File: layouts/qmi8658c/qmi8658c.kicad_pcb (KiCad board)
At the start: 2 copper layers, 3 parts

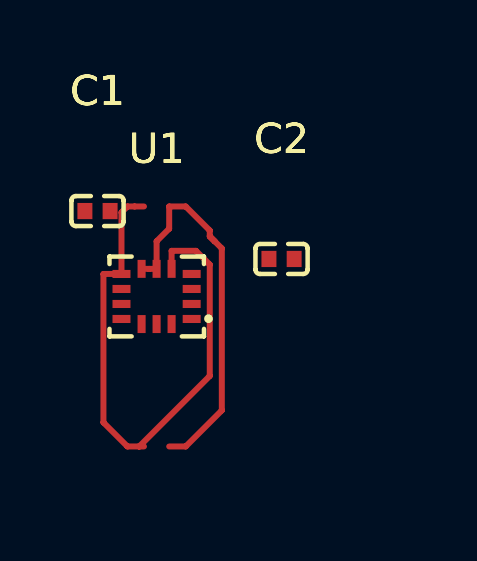
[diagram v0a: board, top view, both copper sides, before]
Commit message: Enhance smart placer with simulated annealing and pre-routing validation
Smart Placer improvements:
- Add simulated annealing refinement (now default) for better wire length optimization
- Add force-directed refinement with improvement safeguard
- Add silkscreen text repositioning to avoid component overlaps
- Significant wire length reductions (e.g., power_filter: 113mm -> 46mm)

Autorouter improvements:
- Add PreRoutingValidator class for pre-flight checks
- Validate unconnected pads, overlapping footprints, unplaced components
- Use pad-based bounds for accurate overlap detection
- Block routing on validation errors with actionable messages

Research:
- Add comprehensive autorouting/autoplacement findings document
- Cover Freerouting Python client, OrthoRoute, DeepPCB, KiCad 9 IPC API
- Document force-directed and simulated annealing algorithms

Cleanup:
- Update .gitignore for DSN/SES files, build artifacts, tools
- Remove stale timestamped build files
- Add parts footprints and symbols

All 10 modules placed and routed successfully.

Co-Authored-By: Claude Opus 4.5 <noreply@anthropic.com>
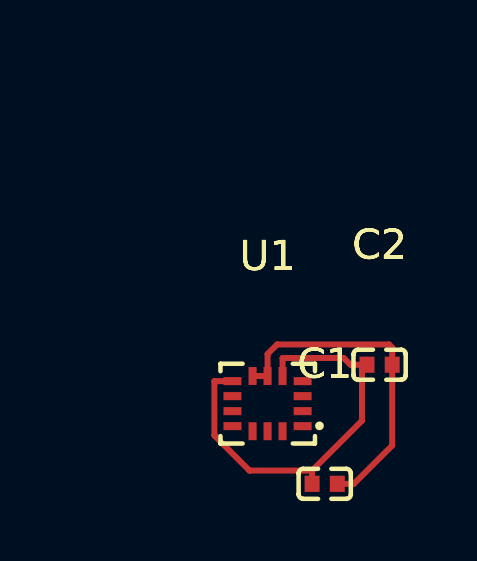
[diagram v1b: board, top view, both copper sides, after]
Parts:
- moved C1 11.8 mm to (105.6, 106.2)
- moved U1 5.14 mm to (103.7, 103.6)
- moved C2 4.81 mm to (107.4, 102.3)
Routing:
- net vcc: track 19.2 -> 14.3 mm
- net gnd: track 13.1 -> 11.2 mm
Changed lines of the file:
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@@
 	(footprint "Samsung_Electro_Mechanics_CL05B104KO5NNNC:C0402"
 		(layer "F.Cu")
-		(at 98.030384 97.152703)
+		(at 105.6041 106.2451)
 		(property "Reference" "C1"
 			(at 0 -4 0)
@@
 	(footprint "QST_QMI8658C:LGA-14_L3.0-W2.5-P0.50-BR"
 		(layer "F.Cu")
-		(at 100 100)
+		(at 103.6991 103.5723)
 		(property "Reference" "U1"
 			(at 0 -4.92 0)
@@
 	(footprint "Samsung_Electro_Mechanics_CL05B104KO5NNNC:C0402"
 		(layer "F.Cu")
-		(at 104.165063 98.75)
+		(at 107.4341 102.2754)
 		(property "Reference" "C2"
 			(at 0 -4 0)
@@
 	)
 	(segment
-		(start 101.3135 98.4783)
-		(end 100.5 98.4783)
-		(width 0.2)
-		(layer "F.Cu")
-		(net 5)
-	)
-	(segment
-		(start 98.2283 104.2)
-		(end 99.0283 105)
-		(width 0.2)
-		(layer "F.Cu")
-		(net 5)
-	)
-	(segment
-		(start 98.83 99.25)
-		(end 98.2283 99.25)
-		(width 0.2)
-		(layer "F.Cu")
-		(net 5)
-	)
-	(segment
-		(start 99.58 105)
-		(end 99.4225 105)
-		(width 0.2)
-		(layer "F.Cu")
-		(net 5)
-	)
-	(segment
-		(start 99.2688 97)
-		(end 99.0283 97)
-		(width 0.2)
-		(layer "F.Cu")
-		(net 5)
-	)
-	(segment
-		(start 99.4225 105)
-		(end 99.0283 105)
-		(width 0.2)
-		(layer "F.Cu")
-		(net 5)
-	)
-	(segment
-		(start 99.4225 105)
-		(end 101.7725 102.65)
-		(width 0.2)
-		(layer "F.Cu")
-		(net 5)
-	)
-	(segment
-		(start 98.83 97.1983)
-		(end 99.0283 97)
-		(width 0.2)
-		(layer "F.Cu")
-		(net 5)
-	)
-	(segment
-		(start 98.2283 99.25)
-		(end 98.2283 104.2)
-		(width 0.2)
-		(layer "F.Cu")
-		(net 5)
-	)
-	(segment
-		(start 100.5 99.08)
-		(end 100.5 98.4783)
-		(width 0.2)
-		(layer "F.Cu")
-		(net 5)
-	)
-	(segment
-		(start 99.58 97)
-		(end 99.2688 97)
-		(width 0.2)
-		(layer "F.Cu")
-		(net 5)
-	)
-	(segment
-		(start 101.7725 98.9373)
-		(end 101.3135 98.4783)
-		(width 0.2)
-		(layer "F.Cu")
-		(net 5)
-	)
-	(segment
-		(start 101.7725 102.65)
-		(end 101.7725 98.9373)
-		(width 0.2)
-		(layer "F.Cu")
-		(net 5)
-	)
-	(segment
-		(start 98.83 99.25)
-		(end 98.83 97.1983)
-		(width 0.2)
-		(layer "F.Cu")
-		(net 5)
-	)
-	(segment
-		(start 101.9388 98.1626)
-		(end 101.7725 97.9963)
+		(start 107.0141 102.2754)
+		(end 106.8453 102.2754)
+		(width 0.2)
+		(layer "F.Cu")
+		(net 5)
+	)
+	(segment
+		(start 104.1991 102.0506)
+		(end 106.2376 102.0506)
+		(width 0.2)
+		(layer "F.Cu")
+		(net 5)
+	)
+	(segment
+		(start 103.096 105.8038)
+		(end 105.1841 105.8038)
+		(width 0.2)
+		(layer "F.Cu")
+		(net 5)
+	)
+	(segment
+		(start 105.1841 105.932)
+		(end 105.1841 105.8038)
+		(width 0.2)
+		(layer "F.Cu")
+		(net 5)
+	)
+	(segment
+		(start 106.8453 104.1426)
+		(end 106.8453 102.2754)
+		(width 0.2)
+		(layer "F.Cu")
+		(net 5)
+	)
+	(segment
+		(start 106.8453 102.2754)
+		(end 106.4624 102.2754)
+		(width 0.2)
+		(layer "F.Cu")
+		(net 5)
+	)
+	(segment
+		(start 105.1841 105.8038)
+		(end 106.8453 104.1426)
+		(width 0.2)
+		(layer "F.Cu")
+		(net 5)
+	)
+	(segment
+		(start 101.9274 102.8223)
+		(end 101.9274 104.6352)
+		(width 0.2)
+		(layer "F.Cu")
+		(net 5)
+	)
+	(segment
+		(start 105.1841 106.2451)
+		(end 105.1841 105.932)
+		(width 0.2)
+		(layer "F.Cu")
+		(net 5)
+	)
+	(segment
+		(start 104.1991 102.6523)
+		(end 104.1991 102.0506)
+		(width 0.2)
+		(layer "F.Cu")
+		(net 5)
+	)
+	(segment
+		(start 102.5291 102.8223)
+		(end 101.9274 102.8223)
+		(width 0.2)
+		(layer "F.Cu")
+		(net 5)
+	)
+	(segment
+		(start 106.2376 102.0506)
+		(end 106.4624 102.2754)
+		(width 0.2)
+		(layer "F.Cu")
+		(net 5)
+	)
+	(segment
+		(start 101.9274 104.6352)
+		(end 103.096 105.8038)
+		(width 0.2)
+		(layer "F.Cu")
+		(net 5)
+	)
+	(segment
+		(start 103.6991 102.6523)
+		(end 103.6991 101.917)
 		(width 0.2)
 		(layer "F.Cu")
@@
 	)
 	(segment
-		(start 100.42 97.7404)
-		(end 100 98.1604)
+		(start 107.8541 102.2754)
+		(end 107.8541 101.7037)
 		(width 0.2)
 		(layer "F.Cu")
@@
 	)
 	(segment
-		(start 100.42 97)
-		(end 100.42 97.7404)
+		(start 103.4491 102.6523)
+		(end 103.6991 102.6523)
 		(width 0.2)
 		(layer "F.Cu")
@@
 	)
 	(segment
-		(start 102.1742 103.7975)
-		(end 102.1742 98.398)
+		(start 107.7507 101.6003)
+		(end 107.8541 101.7037)
 		(width 0.2)
 		(layer "F.Cu")
@@
 	)
 	(segment
-		(start 101.9388 98.1626)
-		(end 101.7725 97.9963)
+		(start 106.0241 106.2451)
+		(end 106.5758 106.2451)
 		(width 0.2)
 		(layer "F.Cu")
@@
 	)
 	(segment
-		(start 101.7725 97.8008)
-		(end 100.9717 97)
+		(start 104.0158 101.6003)
+		(end 107.7507 101.6003)
 		(width 0.2)
 		(layer "F.Cu")
@@
 	)
 	(segment
-		(start 100.42 105)
-		(end 100.9717 105)
+		(start 103.1991 102.6523)
+		(end 103.4491 102.6523)
 		(width 0.2)
 		(layer "F.Cu")
@@
 	)
 	(segment
-		(start 100.42 97)
-		(end 100.9717 97)
+		(start 103.6991 101.917)
+		(end 104.0158 101.6003)
 		(width 0.2)
 		(layer "F.Cu")
@@
 	)
 	(segment
-		(start 100 99.08)
-		(end 99.75 99.08)
+		(start 106.5758 106.2451)
+		(end 107.8541 104.9668)
 		(width 0.2)
 		(layer "F.Cu")
@@
 	)
 	(segment
-		(start 99.75 99.08)
-		(end 99.5 99.08)
-		(width 0.2)
-		(layer "F.Cu")
-		(net 9)
-	)
-	(segment
-		(start 102.1742 98.398)
-		(end 101.9388 98.1626)
-		(width 0.2)
-		(layer "F.Cu")
-		(net 9)
-	)
-	(segment
-		(start 100.9717 105)
-		(end 102.1742 103.7975)
-		(width 0.2)
-		(layer "F.Cu")
-		(net 9)
-	)
-	(segment
-		(start 101.7725 97.9963)
-		(end 101.7725 97.8008)
-		(width 0.2)
-		(layer "F.Cu")
-		(net 9)
-	)
-	(segment
-		(start 100 98.1604)
-		(end 100 99.08)
-		(width 0.2)
-		(layer "F.Cu")
+		(start 107.8541 104.9668)
+		(end 107.8541 102.2754)
+		(width 0.2)
+		(layer "F.Cu")
